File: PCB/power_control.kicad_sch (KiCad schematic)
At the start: 10 parts

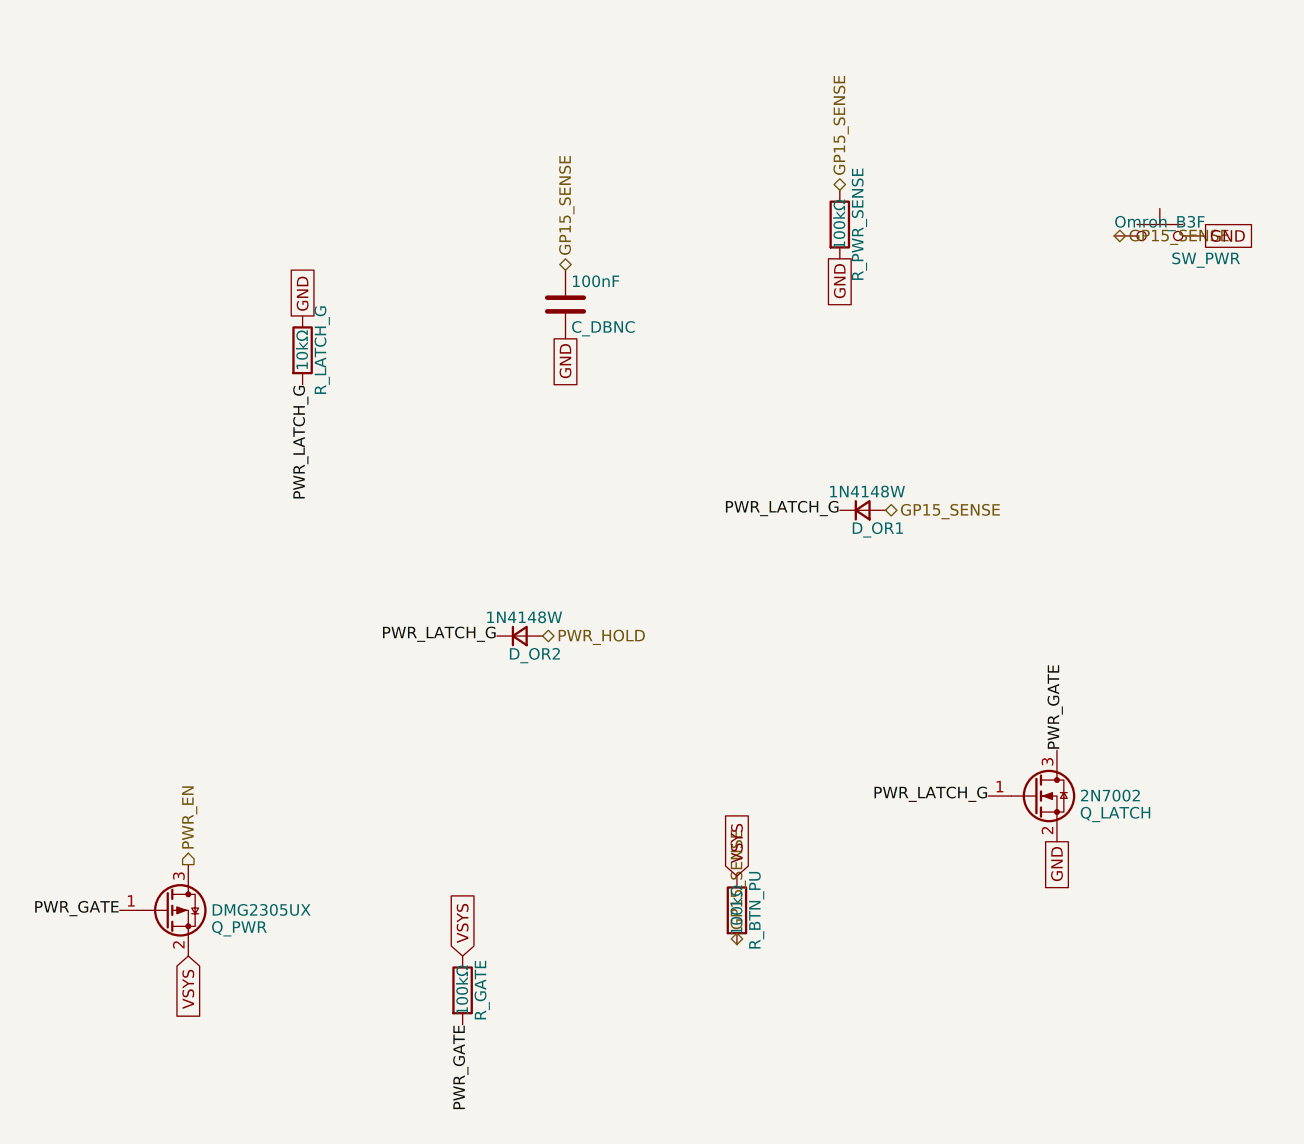
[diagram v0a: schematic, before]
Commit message: refactor: erc is clean
This gets the schematic as clean as it can be.
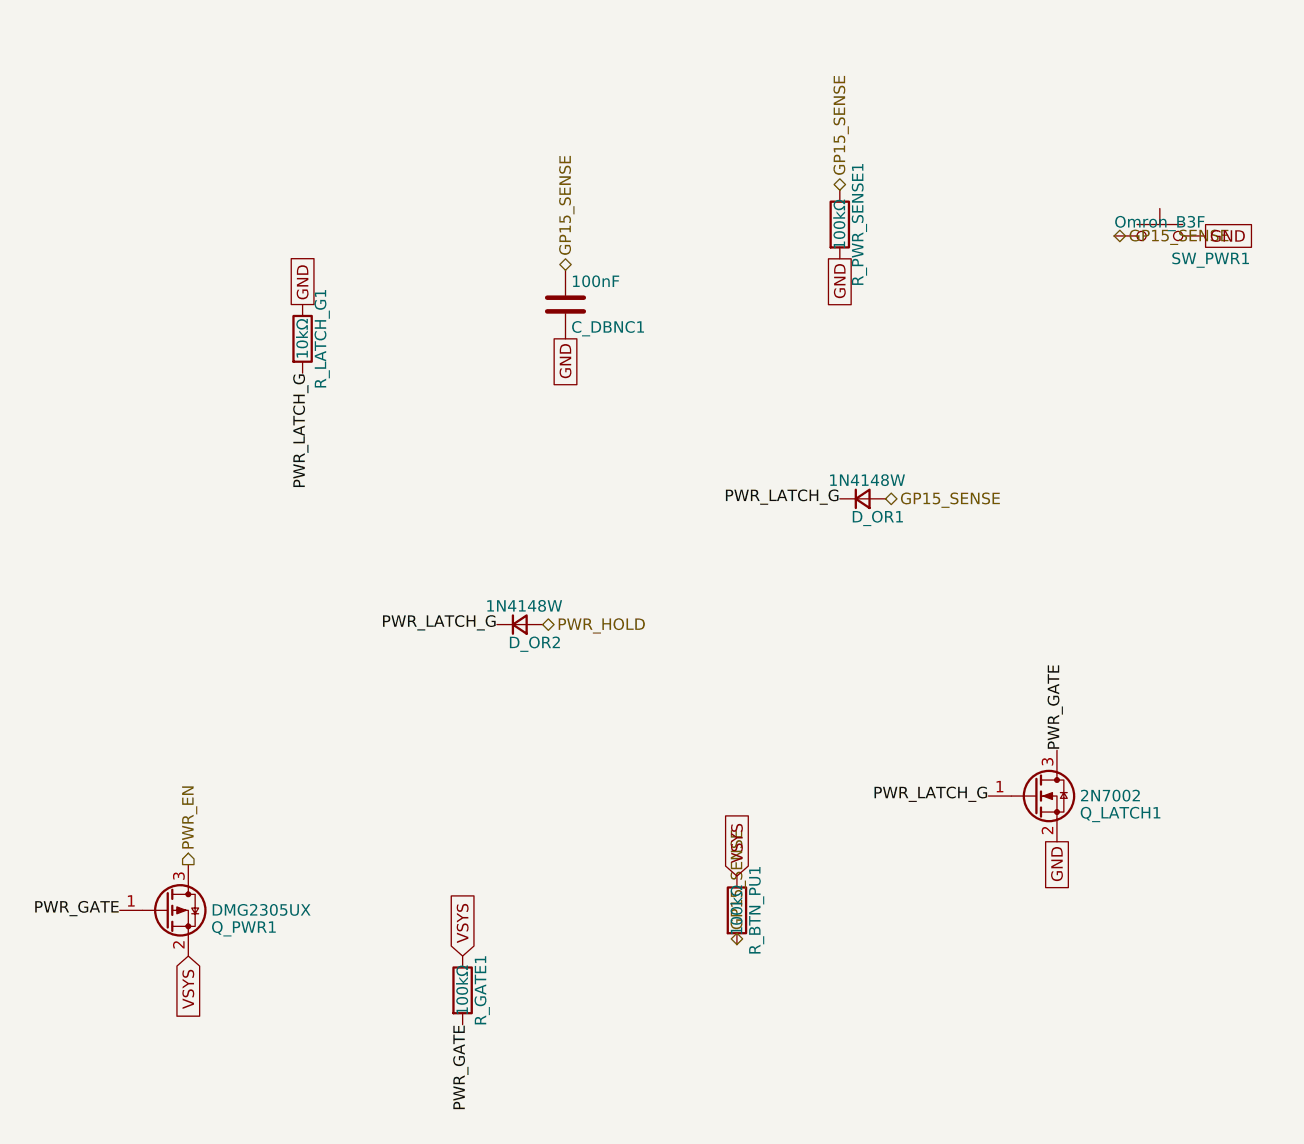
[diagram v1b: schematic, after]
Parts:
- removed C_DBNC: 100nF, symbol Device:C
- removed Q_LATCH: 2N7002, symbol Transistor_FET:Q_NMOS_GSD
- removed Q_PWR: DMG2305UX, symbol Transistor_FET:Q_PMOS_GSD
- removed R_BTN_PU, R_GATE, R_PWR_SENSE: 100kΩ, symbol Device:R
- removed R_LATCH_G: 10kΩ, symbol Device:R
- removed SW_PWR: Omron_B3F, symbol Switch:SW_Push
- added C_DBNC1: 100nF, symbol Device:C
- added Q_LATCH1: 2N7002, symbol Transistor_FET:Q_NMOS_GSD
- added Q_PWR1: DMG2305UX, symbol Transistor_FET:Q_PMOS_GSD
- added R_BTN_PU1, R_GATE1, R_PWR_SENSE1: 100kΩ, symbol Device:R
- added R_LATCH_G1: 10kΩ, symbol Device:R
- added SW_PWR1: Omron_B3F, symbol Switch:SW_Push
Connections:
- net GND: now also C_DBNC1.2, Q_LATCH1.2 (S), R_LATCH_G1.1, R_PWR_SENSE1.2, SW_PWR1.2
- net GP15_SENSE: now also C_DBNC1.1, R_BTN_PU1.2, R_PWR_SENSE1.1, SW_PWR1.1
- net PWR_EN: now also Q_PWR1.3 (D)
- net PWR_GATE: now also Q_LATCH1.3 (D), Q_PWR1.1 (G), R_GATE1.2
- net PWR_LATCH_G: now also Q_LATCH1.1 (G), R_LATCH_G1.2
- net VSYS: now also Q_PWR1.2 (S), R_BTN_PU1.1, R_GATE1.1

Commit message: refactor: switch over to esp32-s3-wroom1 (#13)
This refactors to the esp32-s3 to avoid every problem we encountered with the raspberry pi options.
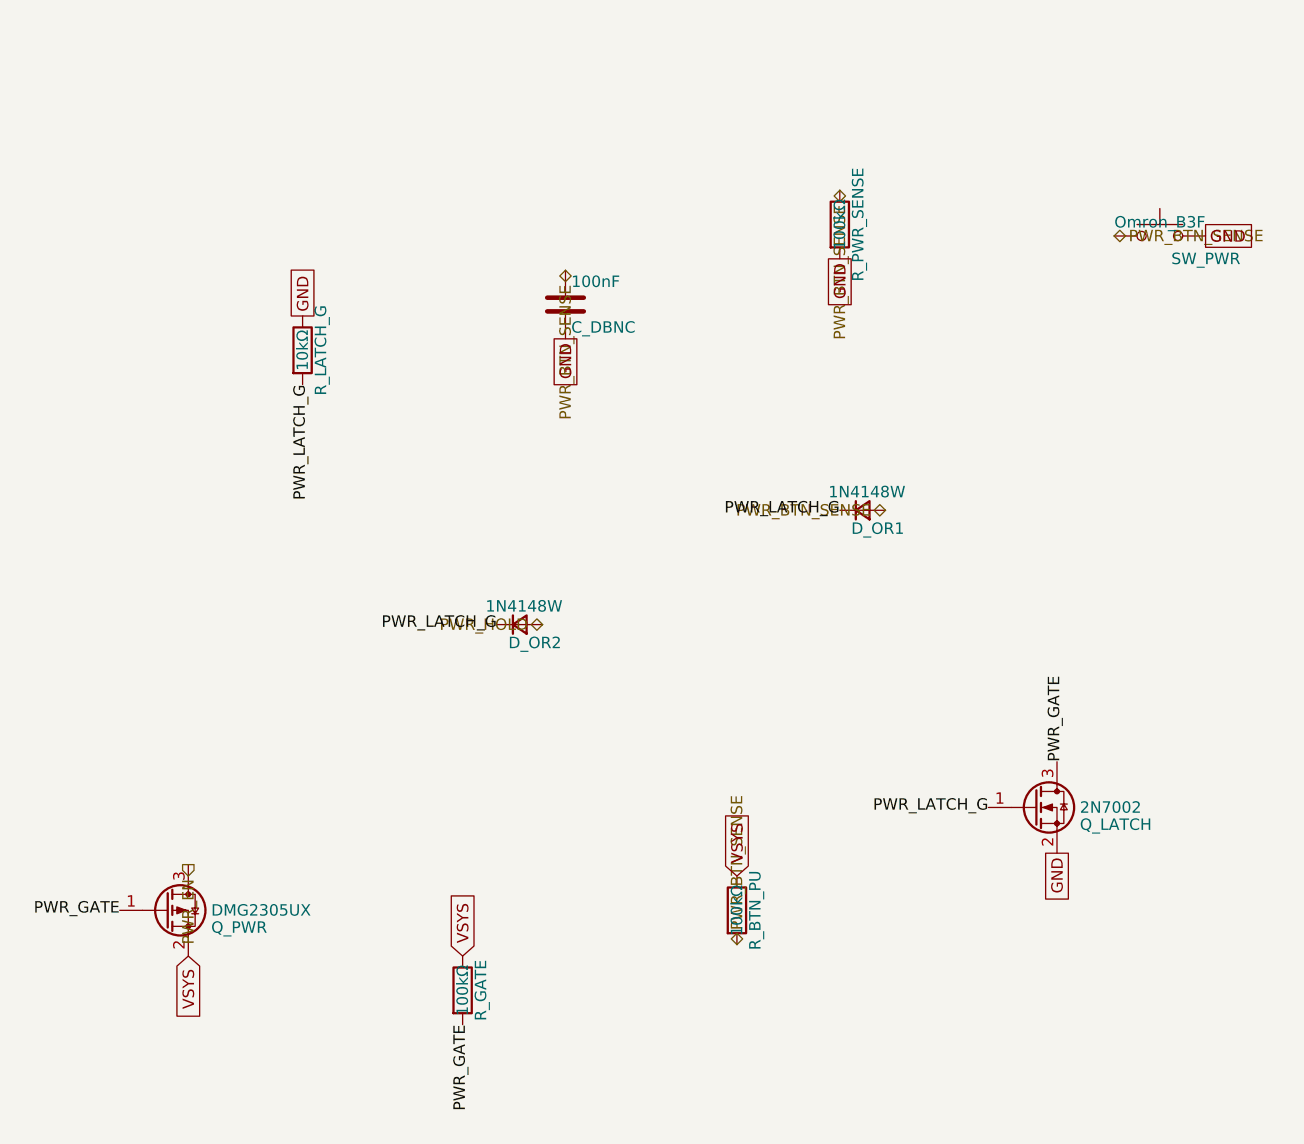
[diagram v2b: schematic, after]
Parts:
- removed C_DBNC1: 100nF, symbol Device:C
- removed Q_LATCH1: 2N7002, symbol Transistor_FET:Q_NMOS_GSD
- removed Q_PWR1: DMG2305UX, symbol Transistor_FET:Q_PMOS_GSD
- removed R_BTN_PU1, R_GATE1, R_PWR_SENSE1: 100kΩ, symbol Device:R
- removed R_LATCH_G1: 10kΩ, symbol Device:R
- removed SW_PWR1: Omron_B3F, symbol Switch:SW_Push
- added C_DBNC: 100nF, Capacitor_SMD:C_0402_1005Metric, symbol Device:C
- added Q_LATCH: 2N7002, Package_TO_SOT_SMD:SOT-23, symbol Transistor_FET:Q_NMOS_GSD
- added Q_PWR: DMG2305UX, Package_TO_SOT_SMD:SOT-23, symbol Transistor_FET:Q_PMOS_GSD
- added R_BTN_PU, R_GATE, R_PWR_SENSE: 100kΩ, Resistor_SMD:R_0402_1005Metric, symbol Device:R
- added R_LATCH_G: 10kΩ, Resistor_SMD:R_0402_1005Metric, symbol Device:R
- added SW_PWR: Omron_B3F, Button_Switch_THT:SW_PUSH_6mm, symbol Switch:SW_Push
- D_OR1, D_OR2: footprint (none) -> Package_TO_SOT_SMD:SOT-23
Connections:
- net GND: now also C_DBNC.2, Q_LATCH.2 (S), R_LATCH_G.1, R_PWR_SENSE.2, SW_PWR.2
- net PWR_EN: now also Q_PWR.3 (D)
- net PWR_GATE: now also Q_LATCH.3 (D), Q_PWR.1 (G), R_GATE.2
- net PWR_LATCH_G: now also Q_LATCH.1 (G), R_LATCH_G.2
- net VSYS: now also Q_PWR.2 (S), R_BTN_PU.1, R_GATE.1
- net GP15_SENSE renamed PWR_BTN_SENSE
- net PWR_BTN_SENSE: now also C_DBNC.1, R_BTN_PU.2, R_PWR_SENSE.1, SW_PWR.1

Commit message: cleanup: annotations and library updates
This is just a task to update the kicad libraries and annotations internally to get that clean ERC.
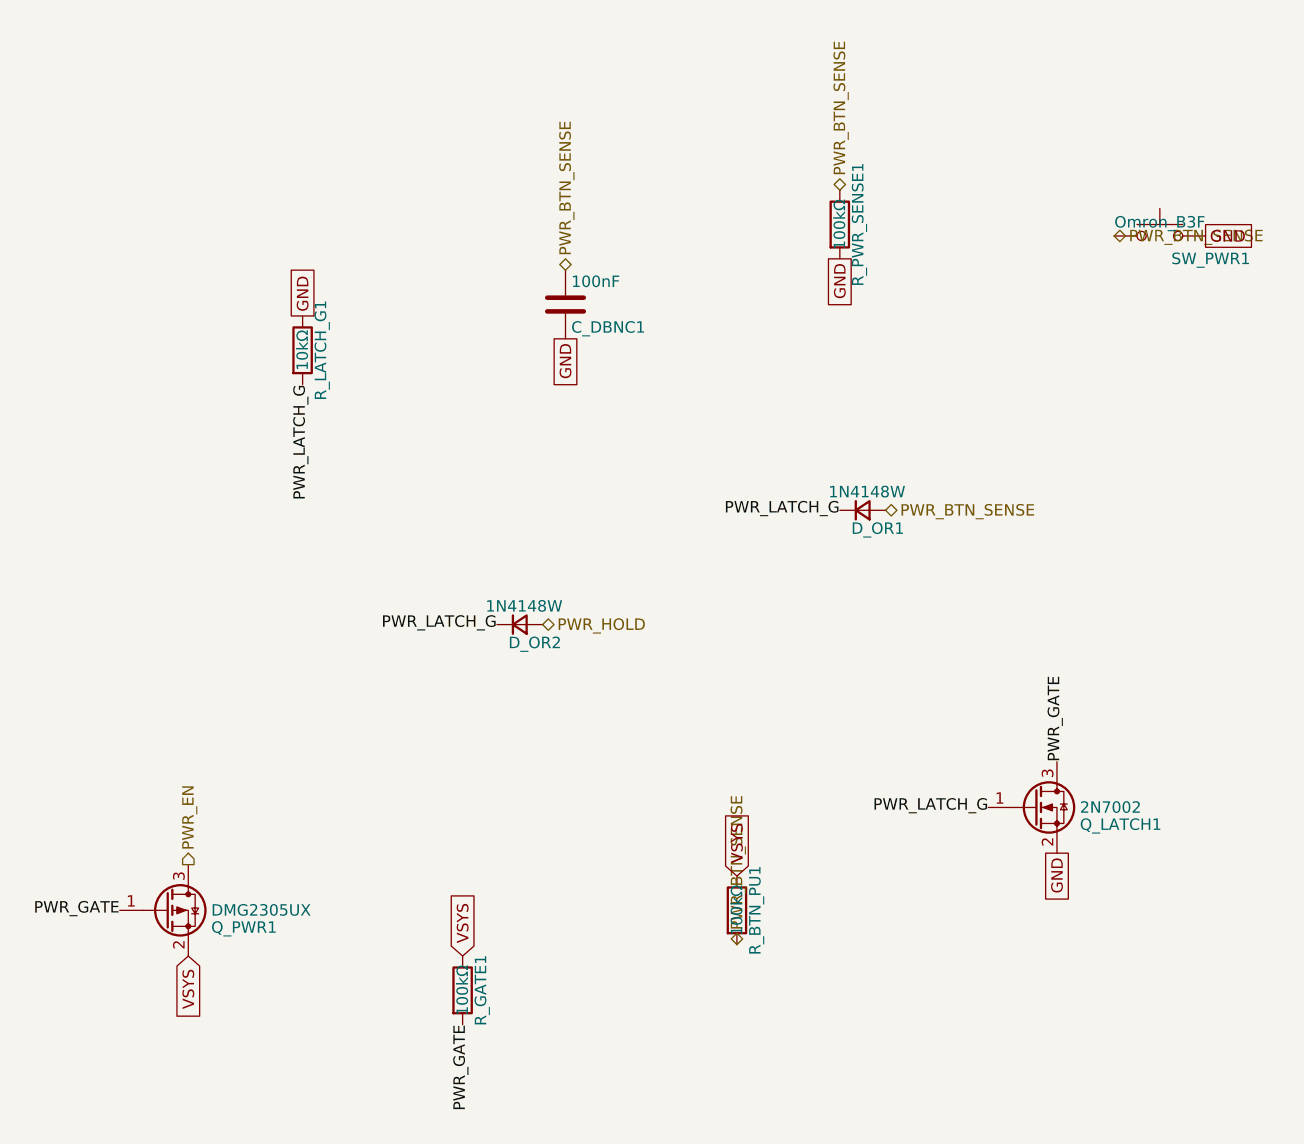
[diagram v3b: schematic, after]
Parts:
- renumbered C_DBNC to C_DBNC1, Q_LATCH to Q_LATCH1, Q_PWR to Q_PWR1, R_BTN_PU to R_BTN_PU1, R_GATE to R_GATE1, R_LATCH_G to R_LATCH_G1, R_PWR_SENSE to R_PWR_SENSE1, SW_PWR to SW_PWR1
